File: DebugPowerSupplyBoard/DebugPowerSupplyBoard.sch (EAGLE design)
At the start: 11 parts, among them IC1 LD117AV33, IC2 7805T

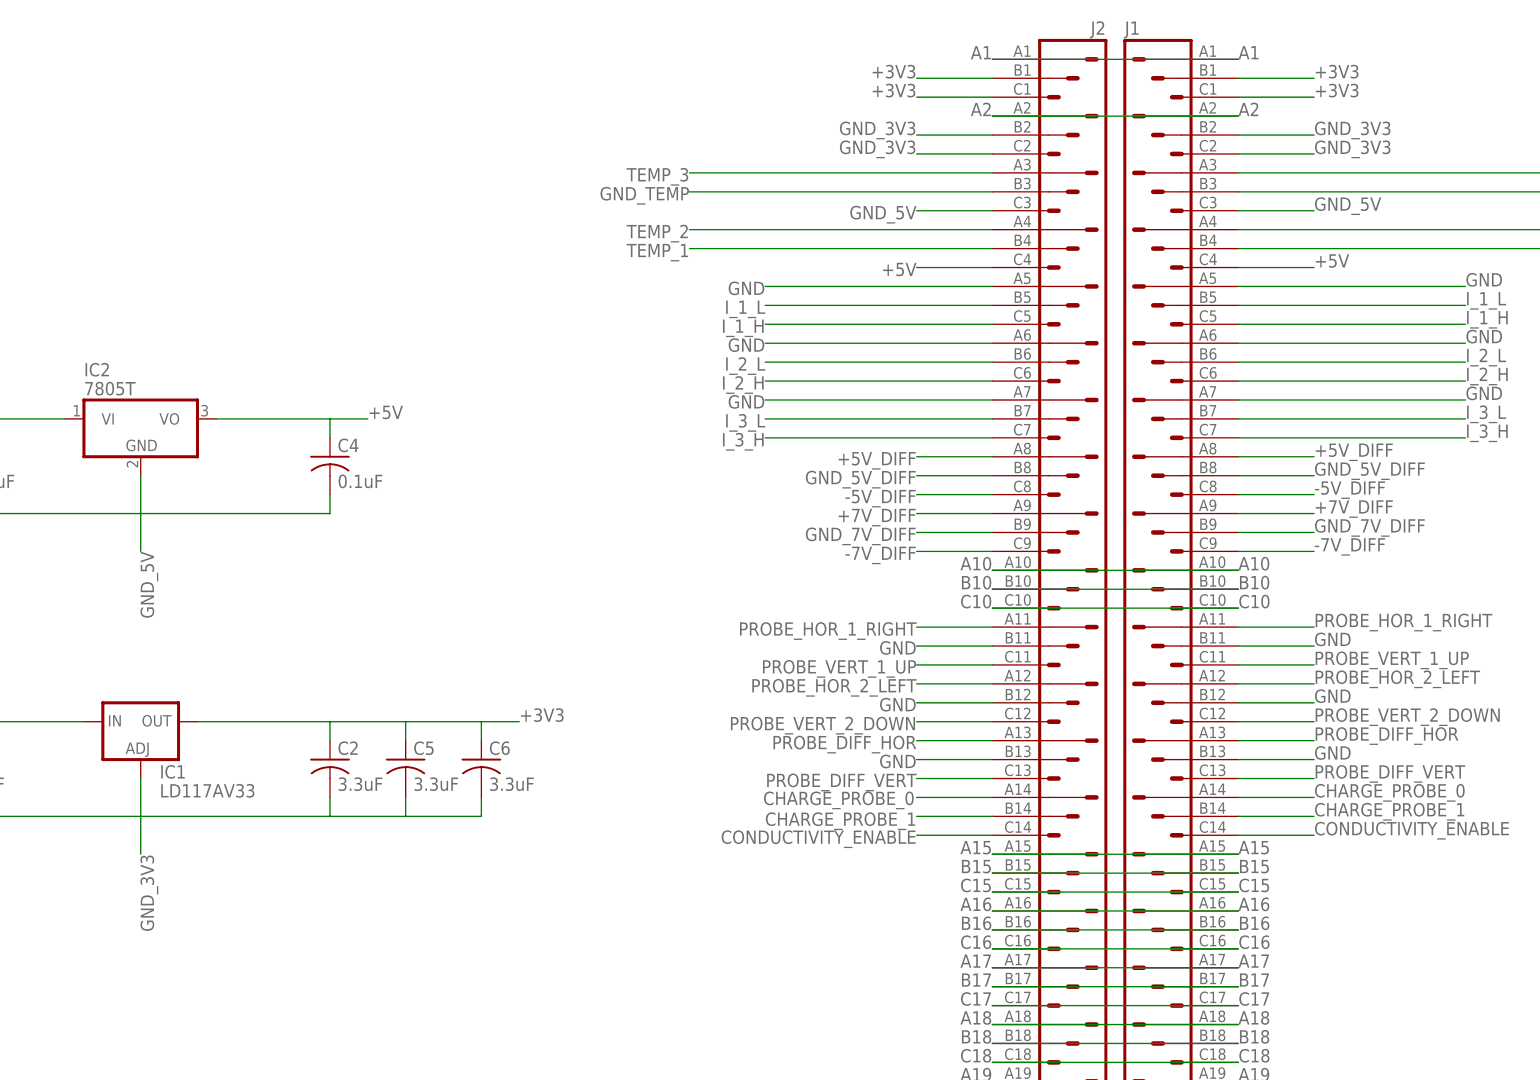
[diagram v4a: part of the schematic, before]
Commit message: All the grounds have the same name now, so Eagle knows to connect them.
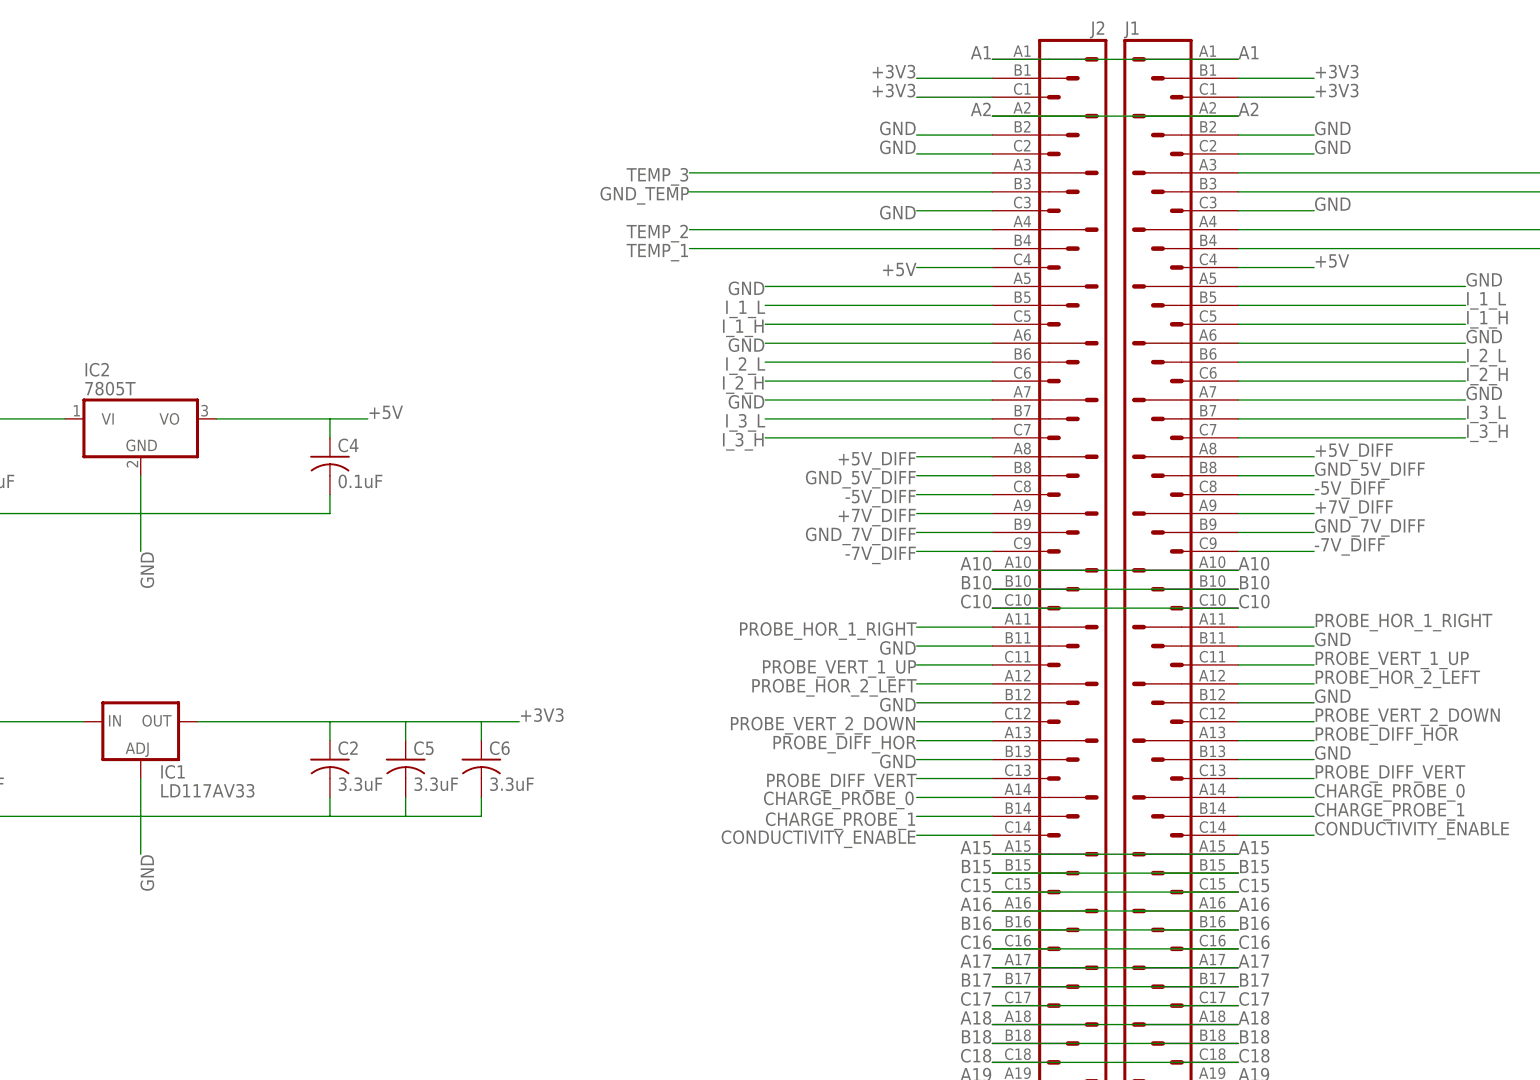
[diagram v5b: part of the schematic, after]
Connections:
- removed net GND_3V3: C1.2, C2.2, C5.2, C6.2, IC1.ADJ, J1.B2, J1.C2, J2.B2, J2.C2
- removed net GND_5V: C3.2, C4.2, IC2.GND, J1.C3, J2.C3
- net GND: now also C1.2, C2.2, C3.2, C4.2, C5.2, C6.2, IC1.ADJ, IC2.GND, J1.B2, J1.C2, J1.C3, J2.B2, J2.C2, J2.C3
